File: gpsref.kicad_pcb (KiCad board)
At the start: 4 copper layers, 79.8 x 47.2 mm, 183 parts, among them J1 SMA, J10 Skedd, J11 I2C_Snoop, J12 GPS_Snoop, J13 Boot, J2 SMA, J3 SMA, J4 SMA, J5 U.Fl, J6 SMA, J7 USB_C_Receptacle_16P, J8 U.Fl, Q1 AO3400A, Q2 AO3401A, T1 MABA-007159-000000, T2 MABA-007159-000000, U1 MAX-M10S, U11 74LVC1G07, U2 LMK05318BRGZR, U21 TMP117xxDRV, U3 TG5032CGN, U31 74LVC1G125, U4 STM32H503KBUx, U41 74CB3Q3306, U5 TPS82084SIL, U6 TPS82084SIL, U7 TPS7A8801RTJR, U8 TPS7A8801RTJR, Y1 32768Hz

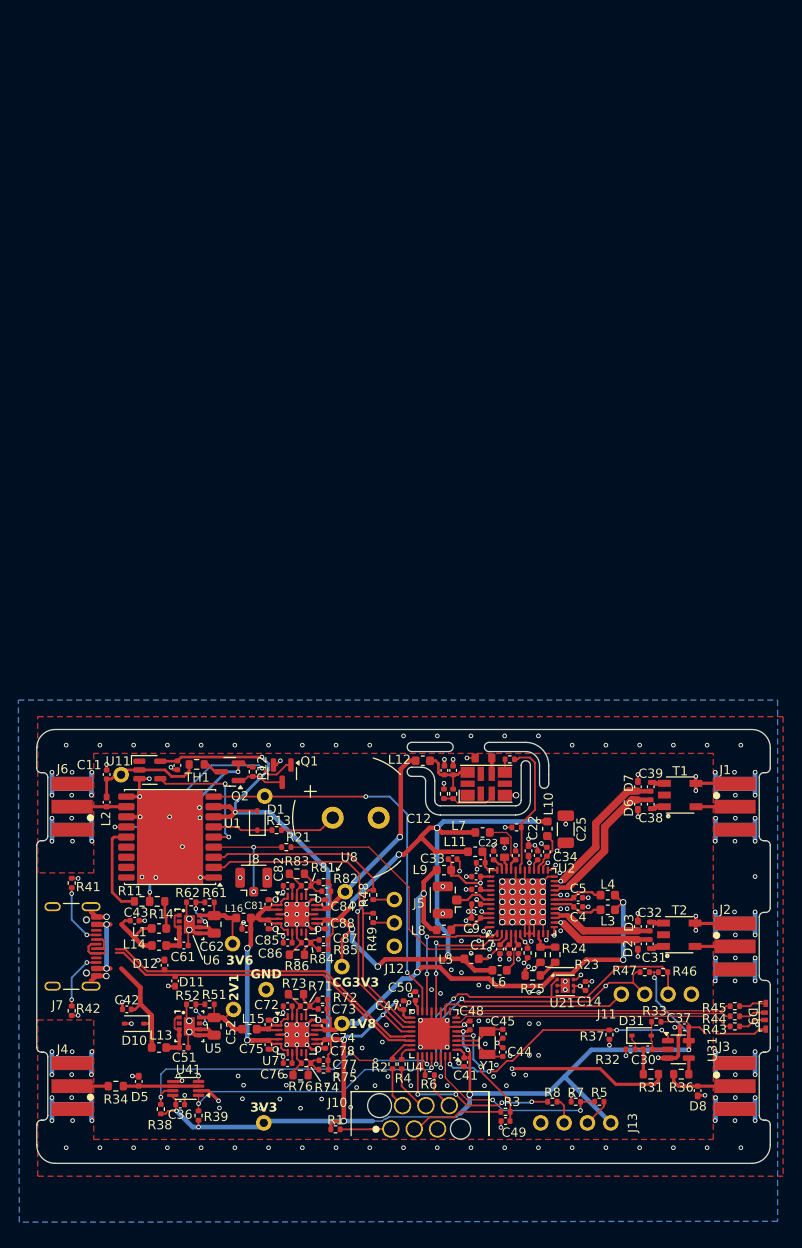
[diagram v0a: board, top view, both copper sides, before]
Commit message: Use impedance matching baluns.
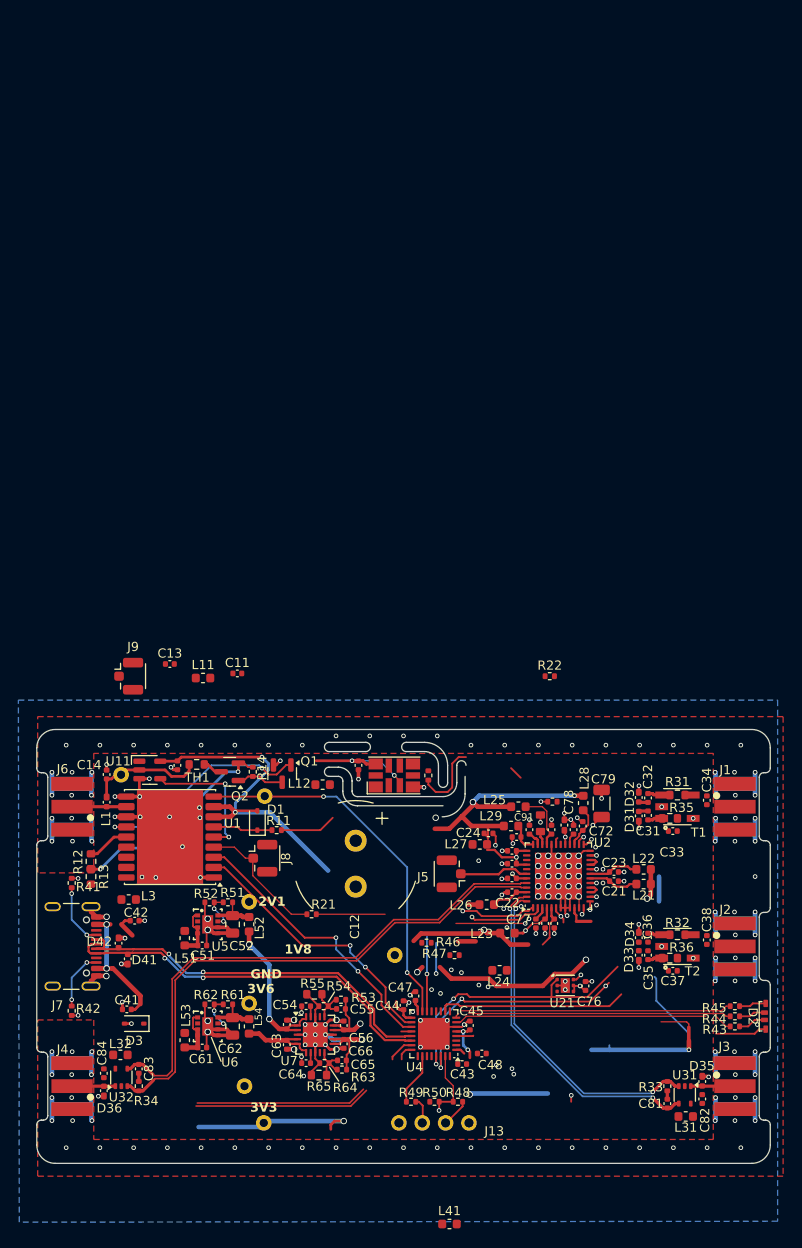
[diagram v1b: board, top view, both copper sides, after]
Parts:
- removed C19, C30, C86: 0u1, Capacitor_SMD:C_0402_1005Metric
- removed C20: 0u1, Parts:C0704
- removed the C31 at (165.5, 99.7)
- removed the C41 at (145.3, 112.6)
- removed the C44 at (149.5, 111.5)
- removed the C45 at (149.5, 109.5)
- removed the C75 at (124.0, 110.7)
- removed C85: 1u, Capacitor_SMD:C_0402_1005Metric
- removed C87: 10n, Capacitor_SMD:C_0402_1005Metric
- removed C88: 10u, Capacitor_SMD:C_0402_1005Metric
- removed the D31 at (164.6, 109.7)
- removed J10: Skedd, Parts:Skedd6
- removed J11: I2C_Snoop, Parts:PinHeader_1x04_P2.54mm_Vertical
- removed J12: GPS_Snoop, Parts:PinHeader_1x03_P2.54mm_Vertical
- removed R1, R2, R3, R4: 100, Resistor_SMD:R_0402_1005Metric
- removed the R23 at (153.6, 100.9)
- removed the R24 at (155.2, 100.9)
- removed R25: 0, Resistor_SMD:R_0603_1608Metric
- removed R28, R29: 1k, Resistor_SMD:R_0402_1005Metric
- removed R37, R38, R39: 100k, Resistor_SMD:R_0402_1005Metric
- removed the R48 at (135.4, 94.4)
- removed the R49 at (135.4, 96.9)
- removed R6: 10k, Resistor_SMD:R_0402_1005Metric
- removed R81, R84: 5k1, Resistor_SMD:R_0402_1005Metric
- removed R82, R85: 15k, Resistor_SMD:R_0402_1005Metric
- removed R83, R86: 82k, Resistor_SMD:R_0603_1608Metric
- removed TP8, TP9: TestPoint_Probe, Parts:TestPoint
- removed U41: 74CB3Q3306, Package_SO:VSSOP-8_2.3x2mm_P0.5mm
- removed U8: TPS7A8801RTJR, Package_DFN_QFN:QFN-20-1EP_4x4mm_P0.5mm_EP2.7x2.7mm
- removed Y1: 32768Hz, Crystal:Crystal_SMD_3215-2Pin_3.2x1.5mm
- added C11: 10u, Capacitor_SMD:C_0402_1005Metric, F.Cu at (120.6, 70.3)
- added C13: 0u1, Capacitor_SMD:C_0402_1005Metric, F.Cu at (113.3, 69.3)
- added C33: 22p, Capacitor_SMD:C_0402_1005Metric, F.Cu at (168.0, 87.5)
- added C34: 0u1, Capacitor_SMD:C_0402_1005Metric, F.Cu at (171.7, 84.1)
- added C35: 0u1, Capacitor_SMD:C_0402_1005Metric, F.Cu at (165.3, 101.0)
- added C43: 10u, Capacitor_SMD:C_0402_1005Metric, F.Cu at (145.1, 112.8)
- added J9: U.Fl, Parts:U.FL_Hirose_U.FL-R-SMT-1_Vertical, F.Cu at (108.8, 70.6)
- added L11: 220, Inductor_SMD:L_0603_1608Metric, F.Cu at (116.9, 70.8)
- added L31: 220, Inductor_SMD:L_0603_1608Metric, F.Cu at (169.4, 118.5)
- added L32: 220, Inductor_SMD:L_0603_1608Metric, F.Cu at (107.9, 111.8)
- added L41: 220, Inductor_SMD:L_0603_1608Metric, F.Cu at (143.7, 130.2)
- added R35: 50, Resistor_SMD:R_0603_1608Metric, F.Cu at (167.7, 86.1)
- added U32: TLV3601DCKR, Package_TO_SOT_SMD:SOT-353_SC-70-5, F.Cu at (108.0, 114.2)
- C31: renamed from C39; value 3n3 -> 0u1
- C32, C38: value 3n3 -> 0u1
- C37: value 0u1 -> 22p
- C81: value 1u -> 10p
- C82: value 0u1 -> 10u
- C83: value 10n -> 10p
- R22: value 200 -> 100
- R32: value 3k3 -> 0; footprint Resistor_SMD:R_0402_1005Metric -> Resistor_SMD:R_0603_1608Metric
- R33: value 100k -> 100
- R34: value 0 -> 100; footprint Resistor_SMD:R_0603_1608Metric -> Resistor_SMD:R_0402_1005Metric
- R36: value 0 -> 50
- R50: renamed from R7; value 100 -> 100k
- T1, T2: value MABA-007159-000000 -> MABA-010247-2R1250
- U31: value 74LVC1G125 -> TLV3601DCKR; footprint Package_TO_SOT_SMD:SOT-23-5 -> Package_TO_SOT_SMD:SOT-353_SC-70-5
- moved C36 54.0 mm to (165.3, 99.0), turned to 90 degrees
- moved C82 50.7 mm to (171.2, 116.6), turned to 90 degrees
- moved C81 48.5 mm to (167.4, 117.1), turned to -90 degrees
- moved R31 30.5 mm to (168.5, 83.5), turned to 0 degrees
- moved C84 30.3 mm to (106.1, 113.8), turned to -90 degrees
- moved R22 30.2 mm to (154.6, 70.6), turned to 0 degrees
- moved C83 28.1 mm to (109.9, 113.3), turned to 90 degrees
- moved R46 25.9 mm to (141.2, 99.6)
- moved R47 20.8 mm to (144.2, 101.0)
- moved C38 16.0 mm to (171.7, 99.3)
- moved J13 15.4 mm to (145.8, 119.2)
- moved R48 15.4 mm to (144.6, 116.9)
- moved R49 15.4 mm to (139.5, 116.9)
- moved R50 15.4 mm to (142.1, 116.9)
- moved C32 14.0 mm to (165.3, 83.8)
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- renumbered C11 to C14, C13 to C15, C4 to C21, C9 to C22, C5 to C23, C33 to C24, C1 to C25, C2 to C27, C3 to C28, C18 to C29, C42 to C41, C43 to C42, C47 to C44, C48 to C45, C50 to C47, C49 to C48, C71 to C53, C72 to C54, C73 to C55, C74 to C56, C46 to C63, C76 to C64, C77 to C65, C78 to C66, C6 to C71, C34 to C72, C7 to C73, C35 to C74, C8 to C75, C14 to C76, C17 to C77, C22 to C78, C25 to C79, C23 to C91, C21 to C92, C24 to C93, D9 to D2, D10 to D3, D6 to D31, D7 to D32, D2 to D33, D3 to D34, D8 to D35, D5 to D36, D11 to D41, D12 to D42, L2 to L1, L3 to L21, L4 to L22, L5 to L23, L6 to L24, L7 to L25, L8 to L26, L9 to L27, L10 to L28, L11 to L29, L1 to L3, L13 to L51, L15 to L52, L14 to L53, L16 to L54, R13 to R11, R11 to R12, R14 to R13, R12 to R14, R26 to R23, R27 to R24, R5 to R48, R8 to R49, R72 to R53, R71 to R54, R73 to R55, R75 to R63, R74 to R64, R76 to R65
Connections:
- net CGEN_1V8 renamed +1V8
- C15 pad 1: +3V3 -> /GPS/VGPS
- C31 pad 1: OUT1_N -> OUT1_P
- C31 pad 2: /Outputs/AC1_N -> Net-(C31-Pad2)
- C32 pad 1: OUT2_N -> OUT1_N
- C32 pad 2: /Outputs/AC2_N -> Net-(C32-Pad2)
- C36 pad 1: +3V3 -> OUT2_P
- C36 pad 2: GND -> Net-(C36-Pad2)
- C37 pad 1: +3V3 -> GND
- C37 pad 2: GND -> Net-(C37-Pad2)
- C38 pad 1: OUT1_P -> /Outputs/Ext2
- C38 pad 2: /Outputs/AC1_P -> Net-(J2-In)
- C44 pad 1: +3V3 -> /CPU/VCPU
- C45 pad 1: +3V3 -> /CPU/VCPU
- C81 pad 1: /Power/In3V3 -> Net-(C81-Pad1)
- C81 pad 2: GND -> OUT3_N
- C82 pad 1: Net-(U8A-NR_SS1) -> Net-(U31-V+)
- C83 pad 1: TCXO_3V3 -> Net-(C83-Pad1)
- C83 pad 2: /Power/FbTC3 -> OUT4_N
- C84 pad 1: TCXO_3V3 -> Net-(U32-V+)
- D1 pad 2: +3V3 -> /GPS/VGPS
- D33 pad 1: OUT2_P -> OUT2_N
- D34 pad 1: OUT2_N -> OUT2_P
- D36 pad 1: Net-(D5-A1) -> /Outputs/Ext4
- J1 pad 1: /Outputs/Ext1 -> Net-(J1-In)
- J13 pad 3: /CPU/dRX -> /CPU/dTX
- J2 pad 1: /Outputs/Ext2 -> Net-(J2-In)
- J4 pad 1: /Outputs/Conn4 -> /Outputs/Ext4
- L12 pad 1: TCXO_3V3 -> +3V3
- L23 pad 1: CGEN_3V3 -> +3V3
- L24 pad 1: CGEN_3V3 -> +3V3
- L25 pad 1: CGEN_3V3 -> +3V3
- L28 pad 1: CGEN_3V3 -> +3V3
- L29 pad 1: CGEN_3V3 -> +3V3
- R22 pad 1: GND -> Net-(J9-In)
- R22 pad 2: /Clocking/GPSCLKLO -> /Clocking/SecRefLo
- R31 pad 1: OUT3 -> Net-(C32-Pad2)
- R31 pad 2: Net-(D31-K) -> /Outputs/Ext1
- R32 pad 1: GND -> Net-(C36-Pad2)
- R32 pad 2: Net-(D31-K) -> /Outputs/Ext2
- R33 pad 1: Net-(D31-A) -> OUT3_P
- R33 pad 2: +3V3 -> Net-(C81-Pad1)
- R34 pad 1: Net-(D5-A1) -> OUT4_P
- R34 pad 2: /Outputs/Conn4 -> Net-(C83-Pad1)
- R36 pad 1: Net-(R36-Pad1) -> Net-(C37-Pad2)
- R36 pad 2: /Outputs/Ext3 -> Net-(C35-Pad2)
- R46 pad 2: +3V3 -> /CPU/VCPU
- R47 pad 2: +3V3 -> /CPU/VCPU
- R49 pad 1: /CPU/dRX -> /CPU/dTX
- R49 pad 2: /CPU/DBG_RX -> /CPU/DBG_TX
- T1 pad 1: /Outputs/AC1_P -> Net-(C31-Pad2)
- T1 pad 2: unconnected-(T1-Pad2) -> GND
- T1 pad 3: /Outputs/AC1_N -> Net-(C32-Pad2)
- T1 pad 4: GND -> /Outputs/Ext1
- T1 pad 5: /Outputs/Ext1 -> GND
- T2 pad 1: /Outputs/AC2_P -> Net-(C35-Pad2)
- T2 pad 2: unconnected-(T2-Pad2) -> GND
- T2 pad 3: /Outputs/AC2_N -> Net-(C36-Pad2)
- T2 pad 4: GND -> /Outputs/Ext2
- T2 pad 5: /Outputs/Ext2 -> GND
- U1 pad 7: +3V3 -> /GPS/VGPS
- U1 pad 8: +3V3 -> /GPS/VGPS
- U11 pad 5: +3V3 -> /GPS/VGPS
- U2 pad 2: STATUS1 -> FDEC
- U2 pad 30: GND -> FINC
- U2 pad 44: unconnected-(U2-OUT6_N-Pad44) -> OUT4_N
- U2 pad 45: OUT4 -> OUT4_P
- U2 pad 47: unconnected-(U2-OUT7_N-Pad47) -> OUT3_N
- U2 pad 48: OUT3 -> OUT3_P
- U3 pad 3: Net-(U3A-OE) -> /Clocking/VCC_XO
- U3 pad 7: /Clocking/XO_Filter -> unconnected-(U3A-Filter-Pad7)
- U31 pad 1: EN_OUT3 -> /Outputs/Ext3
- U31 pad 2: Net-(D31-A) -> GND
- U31 pad 3: GND -> OUT3_P
- U31 pad 4: Net-(R36-Pad1) -> OUT3_N
- U31 pad 5: +3V3 -> Net-(U31-V+)
- U4 pad 1: +3V3 -> /CPU/VCPU
- U4 pad 11: GND -> FINC
- U4 pad 12: STATUS1 -> GND
- U4 pad 13: GND -> FDEC
- U4 pad 17: +3V3 -> /CPU/VCPU
- U4 pad 2: /CPU/X32In -> unconnected-(U4-PC14-Pad2)
- U4 pad 20: +3V3 -> /CPU/VCPU
- U4 pad 23: /CPU/SWDIO -> unconnected-(U4-PA13(JTMS-Pad23)
- U4 pad 24: /CPU/SWCLK -> unconnected-(U4-PA14(JTCK-Pad24)
- U4 pad 25: /CPU/DBG_RX -> unconnected-(U4-PA15(JTDI)-Pad25)
- U4 pad 27: EN_OUT4 -> unconnected-(U4-PB4(NJTRST)-Pad27)
- U4 pad 28: EN_REF2 -> unconnected-(U4-PB5-Pad28)
- U4 pad 3: /CPU/X32Out -> unconnected-(U4-PC15-Pad3)
- U4 pad 32: EN_OUT3 -> unconnected-(U4-PB8-Pad32)
- U4 pad 5: +3V3 -> /CPU/VCPU
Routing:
- net CGEN_3V3: track 84.6 -> 0.00 mm, vias 7 -> 0
- net OUT4_P: track 0.00 -> 78.0 mm
- net +3V3: track 225.0 -> 147.4 mm, vias 14 -> 9
- net OUT4_N: track 0.00 -> 77.4 mm
- net +1V8: track 68.4 -> 12.6 mm, vias 4 -> 2
- net GND: track 217.5 -> 165.5 mm, vias 304 -> 236
- net SecRef: track 50.0 -> 0.00 mm, vias 2 -> 0
- net OUT4: track 44.5 -> 0.00 mm, vias 2 -> 0
- net /GPS/VGPS: track 0.00 -> 39.4 mm, vias 0 -> 2
- net OUT3_N: track 0.00 -> 37.4 mm, vias 0 -> 2
- net EN_OUT4: track 36.4 -> 0.00 mm, vias 4 -> 0
- net OUT3_P: track 0.00 -> 36.3 mm, vias 0 -> 2
- net OUT3: track 34.8 -> 0.00 mm, vias 2 -> 0
- net EN_REF2: track 29.9 -> 0.00 mm, vias 2 -> 0
- net EN_OUT3: track 27.6 -> 0.00 mm, vias 4 -> 0
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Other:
- outline, holes or cut-outs redrawn
- board text removed: "CG3V3"

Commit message: Put the two long differential lines on the front.
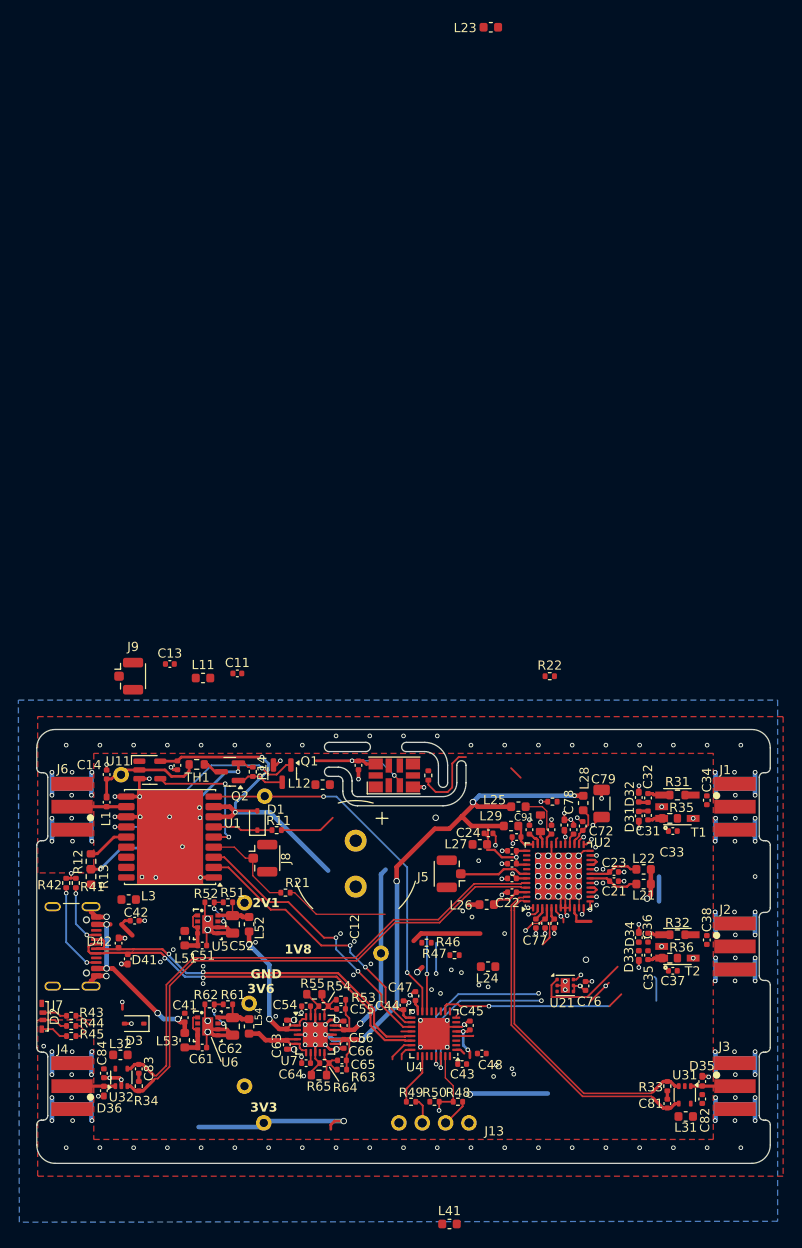
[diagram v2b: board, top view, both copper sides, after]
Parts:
- moved L23 98.6 mm to (148.2, 0.00)
- moved D2 78.8 mm to (99.3, 107.6), turned to 90 degrees
- moved R45 72.3 mm to (102.5, 109.8), turned to 0 degrees
- moved R43 72.2 mm to (102.5, 107.5), turned to 0 degrees
- moved R44 72.2 mm to (102.5, 108.7), turned to 0 degrees
- moved R42 13.9 mm to (102.0, 93.1), turned to -90 degrees
- moved C41 6.36 mm to (114.9, 107.8), turned to -90 degrees
- moved R21 3.69 mm to (125.9, 94.2)
- moved TP6 1.51 mm to (136.2, 100.8)
- moved L24 1.31 mm to (147.9, 102.2)
- moved TP4 0.51 mm to (121.4, 95.2)
- moved R41 0.45 mm to (103.0, 93.1)
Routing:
- net /CPU/Red: track 29.5 -> 1.15 mm
- net /CPU/Green: track 29.1 -> 1.42 mm
- net /CPU/Blue: track 29.1 -> 2.00 mm
- net +3V3: track 147.4 -> 122.1 mm, vias 9 -> 8
- net OUT4_P: track 78.0 -> 58.0 mm
- net (no net): track 23.5 -> 3.62 mm
- net OUT4_N: track 77.4 -> 58.0 mm
- net +1V8: track 12.6 -> 30.5 mm
- net I2C_SDA: track 32.0 -> 26.5 mm
- net VBus: track 18.3 -> 23.4 mm, vias 2 -> 4
- net GPSCLK: track 14.3 -> 10.5 mm
- net /Clocking/GPSCLKLO: track 21.2 -> 25.0 mm, vias 2 -> 1
- net /CPU/CC2: track 6.45 -> 10.2 mm
- net GND: track 165.5 -> 168.4 mm, vias 236 -> 242
- net I2C_SCL: track 37.6 -> 36.1 mm
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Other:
- outline, holes or cut-outs redrawn

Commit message: Routing basically done.
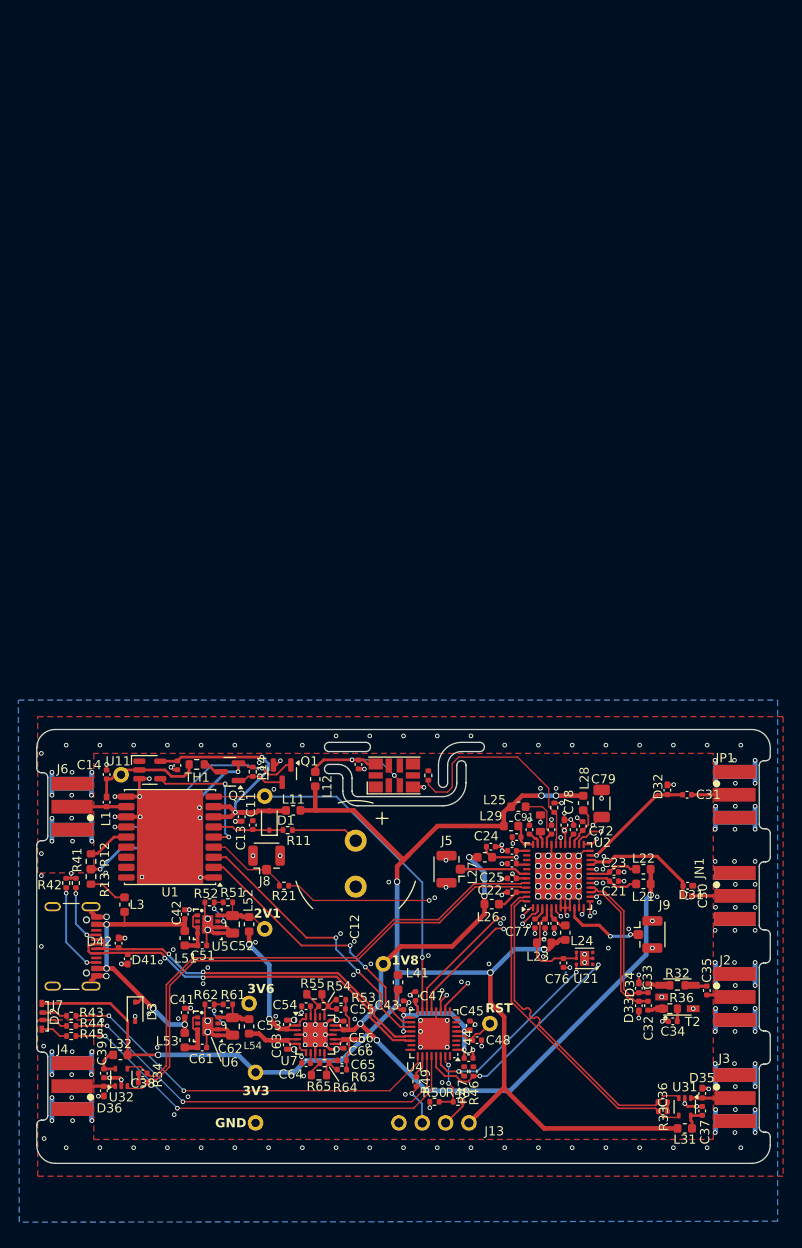
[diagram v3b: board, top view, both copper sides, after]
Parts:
- removed the C33 at (168.0, 87.5)
- removed the C34 at (171.7, 84.1)
- removed R22: 100, Resistor_SMD:R_0402_1005Metric
- removed R31: 0, Resistor_SMD:R_0603_1608Metric
- removed R35: 50, Resistor_SMD:R_0603_1608Metric
- removed T1: MABA-010247-2R1250, Parts:XFMR_MABA-007159-000000
- added JN1: SMA, Parts:SMA_EdgeMount, F.Cu at (174.9, 94.5)
- added TP8: TestPoint_Probe, Parts:TestPoint, F.Cu at (148.1, 108.4)
- moved L23 99.8 mm to (154.0, 99.6), turned to 180 degrees
- moved J9 63.1 mm to (165.3, 98.7)
- moved L41 26.9 mm to (138.1, 103.9), turned to -90 degrees
- moved C13 19.7 mm to (122.3, 86.8), turned to 90 degrees
- moved L11 17.4 mm to (126.7, 85.2), turned to 180 degrees
- moved C11 15.6 mm to (121.1, 85.9), turned to -90 degrees
- moved R46 14.9 mm to (146.3, 113.6), turned to 90 degrees
- moved R47 12.7 mm to (145.3, 113.6), turned to 90 degrees
- moved C30 9.73 mm to (169.6, 94.5), turned to 0 degrees
- moved D31 9.27 mm to (169.6, 93.4), turned to 0 degrees
- moved L24 9.18 mm to (156.3, 98.5), turned to 90 degrees
- moved C44 9.12 mm to (145.8, 112.2), turned to 0 degrees
- moved C43 9.04 mm to (138.7, 106.4), turned to 90 degrees
- moved TP7 5.57 mm to (122.6, 113.7)
- moved C32 5.50 mm to (165.3, 106.5)
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- renumbered C31 to C30, C32 to C31, C35 to C32, C36 to C33, C37 to C34, C38 to C35, C81 to C36, C82 to C37, C83 to C38, C84 to C39, J1 to JP1
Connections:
- C31 pad 2: Net-(C32-Pad2) (its old number) -> Net-(JP1-In)
- C32 pad 1: OUT2_N -> OUT2_P
- C33 pad 1: OUT2_P -> OUT2_N
- D33 pad 1: OUT2_N -> OUT2_P
- D34 pad 1: OUT2_P -> OUT2_N
- J9 pad 1: Net-(J9-In) -> /Clocking/SecRef
- JP1 pad 1: Net-(J1-In) -> Net-(JP1-In)
- U2 pad 10: /Clocking/SecRefLo -> /Clocking/SecRef
- U4 pad 25: unconnected-(U4-PA15(JTDI)-Pad25) -> /CPU/Blue
- U4 pad 27: unconnected-(U4-PB4(NJTRST)-Pad27) -> /CPU/Green
- U4 pad 28: unconnected-(U4-PB5-Pad28) -> /CPU/Red
- U4 pad 6: GND -> unconnected-(U4-PA0-Pad6)
- U4 pad 7: /CPU/Blue -> unconnected-(U4-PA1-Pad7)
- U4 pad 8: /CPU/Green -> unconnected-(U4-PA2-Pad8)
- U4 pad 9: /CPU/Red -> unconnected-(U4-PA3-Pad9)
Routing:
- net +1V8: track 30.5 -> 86.1 mm, vias 2 -> 5
- net +3V3: track 122.1 -> 170.4 mm, vias 8 -> 7
- net /CPU/Red: track 1.15 -> 46.5 mm, vias 0 -> 2
- net /CPU/Green: track 1.42 -> 45.6 mm, vias 0 -> 2
- net /CPU/Blue: track 2.00 -> 42.5 mm, vias 0 -> 2
- net FINC: track 0.00 -> 36.6 mm, vias 0 -> 2
- net I2C_SDA: track 26.5 -> 43.3 mm, vias 5 -> 3
- net OUT2_P: track 2.90 -> 18.4 mm
- net OUT2_N: track 1.62 -> 17.1 mm
- net /Clocking/XO_P: track 10.3 -> 25.0 mm
- net OUT1_P: track 2.63 -> 13.9 mm
- net OUT1_N: track 3.92 -> 15.0 mm
- net I2C_SCL: track 36.1 -> 46.8 mm
- net /CPU/VCPU: track 9.94 -> 20.2 mm, vias 2 -> 4
- net FDEC: track 8.05 -> 17.7 mm
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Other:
- outline, holes or cut-outs redrawn
- board text added: "RST"

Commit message: DRC clean-up.
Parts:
- U2: footprint Package_DFN_QFN:QFN-48-1EP_7x7mm_P0.5mm_EP5.1x5.1mm -> Parts:QFN-48-1EP_7x7mm_P0.5mm_EP5.1x5.1mm
- U4: footprint Package_DFN_QFN:QFN-32-1EP_5x5mm_P0.5mm_EP3.45x3.45mm -> Parts:QFN-32-1EP_5x5mm_P0.5mm_EP3.45x3.45mm
- U7: footprint Package_DFN_QFN:QFN-20-1EP_4x4mm_P0.5mm_EP2.7x2.7mm -> Parts:QFN-20-1EP_4x4mm_P0.5mm_EP2.7x2.7mm
- moved C24 0.05 mm to (148.2, 89.1)
- renumbered C37 to C3
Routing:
- net /Clocking/XO: track 0.00 -> 1.98 mm
- net /CPU/VCPU: track 20.2 -> 22.1 mm
- net /Power/3V6: track 4.88 -> 6.59 mm
- net GND: track 166.8 -> 168.1 mm, vias 284 -> 290
- net +3V3: track 170.4 -> 171.4 mm, vias 7 -> 8
- net I2C_SCL: track 46.8 -> 47.4 mm
- net unconnected-(U4-PA14(JTCK-Pad24): track 0.61 -> 0.00 mm
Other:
- outline, holes or cut-outs redrawn
